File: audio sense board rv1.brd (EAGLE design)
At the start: 80 x 26.7 mm, 32 parts, among them IC2 TSOP38238, J1 PJRAN1X1U01X, J2 Debug Jumper, J4 PJRAN1X1U01X, Q1 2N3904, Q2 2N3904

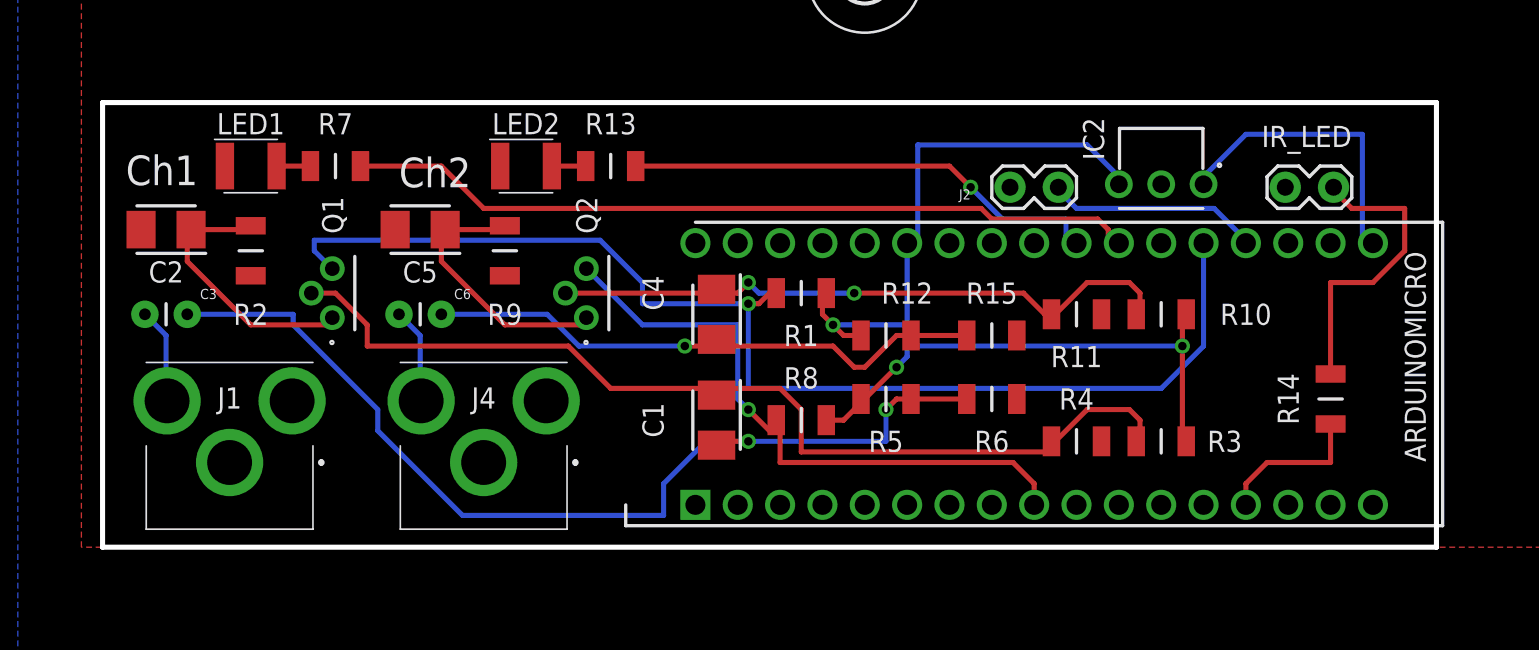
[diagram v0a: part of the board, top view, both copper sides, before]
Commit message: update resistors, corners
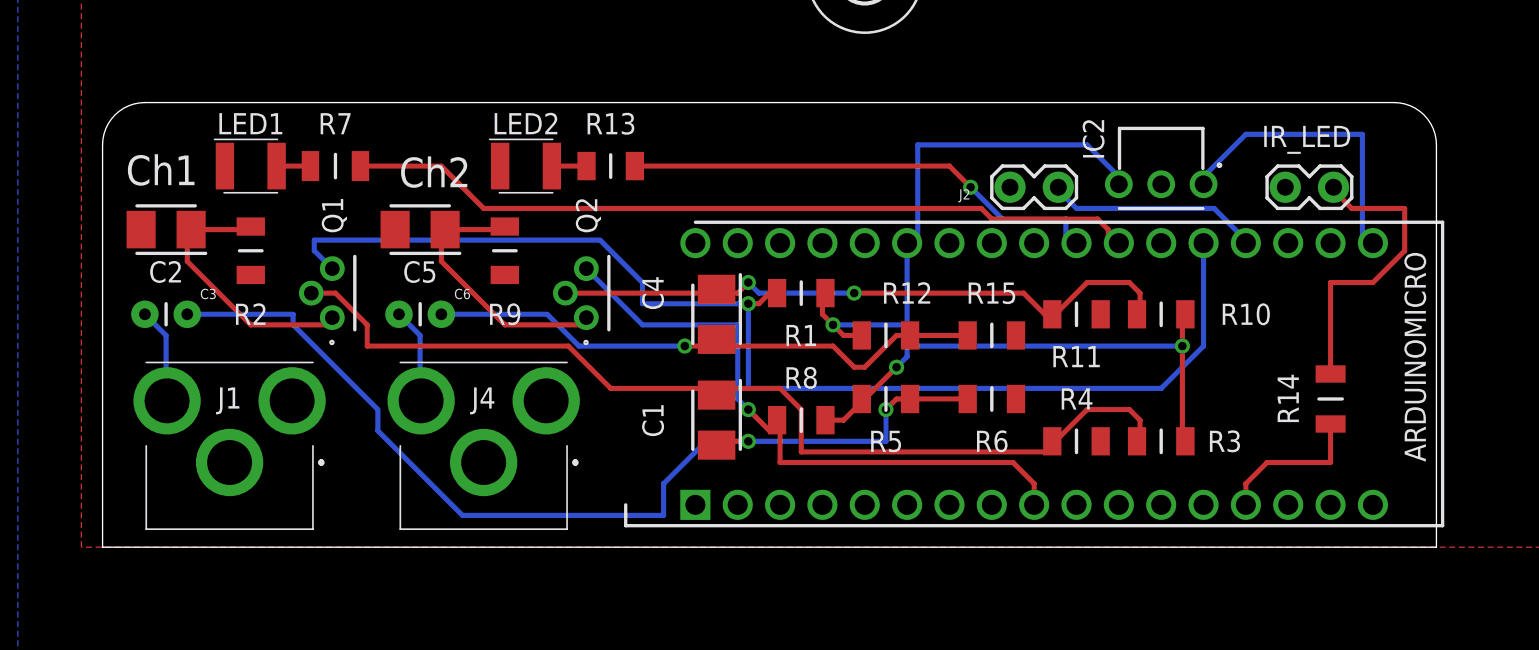
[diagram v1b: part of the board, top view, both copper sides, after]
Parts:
- R1, R10, R3, R8: device Samac Populated:RESC3216X60N@1 -> Samac Populated:RESC3116X70N
- R11, R12, R15, R2, R4, R5, R6, R9: device Samac Populated:RESC3216X60N -> Samac Populated:RESC3116X70N
- R13: value CRCW1206100RJNEAC -> ERJ8GEYJ101V; device Samac Populated:RESC3216X60N -> Samac Populated:RESC3116X70N
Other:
- outline, holes or cut-outs redrawn

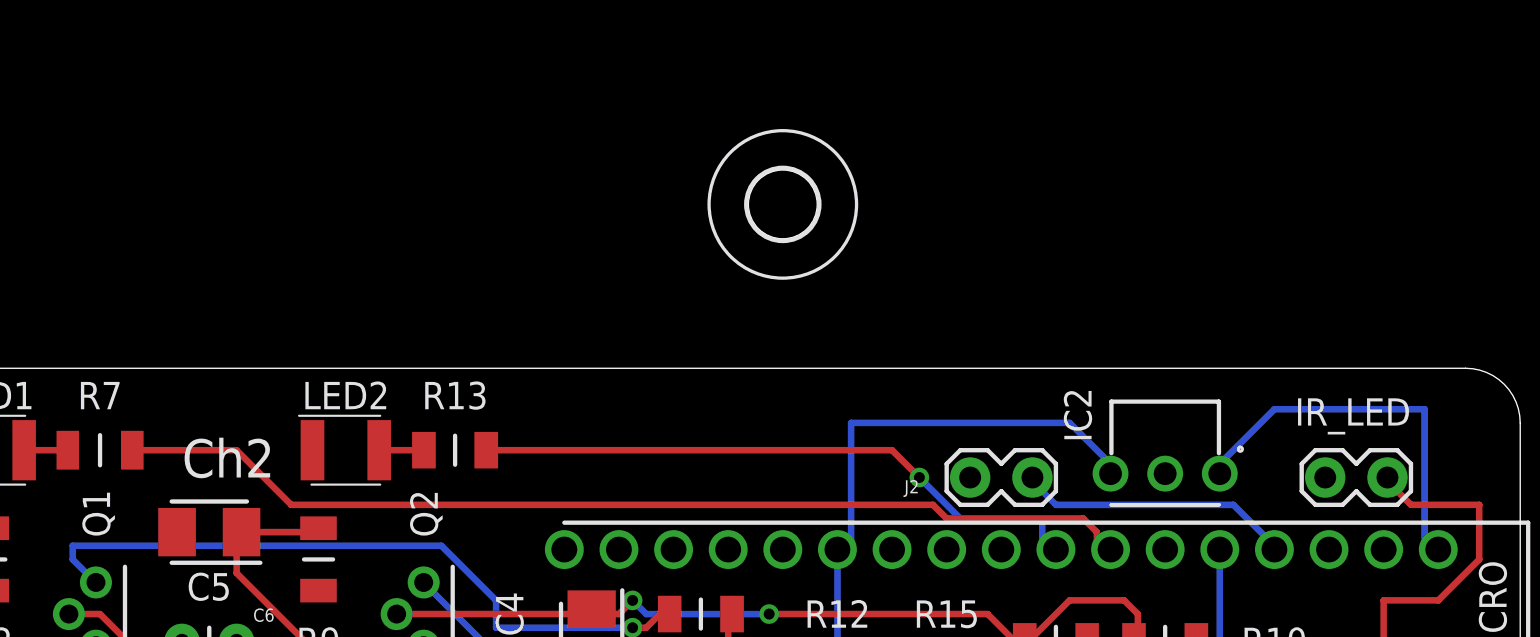
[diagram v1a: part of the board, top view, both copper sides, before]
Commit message: match LED names to channel names
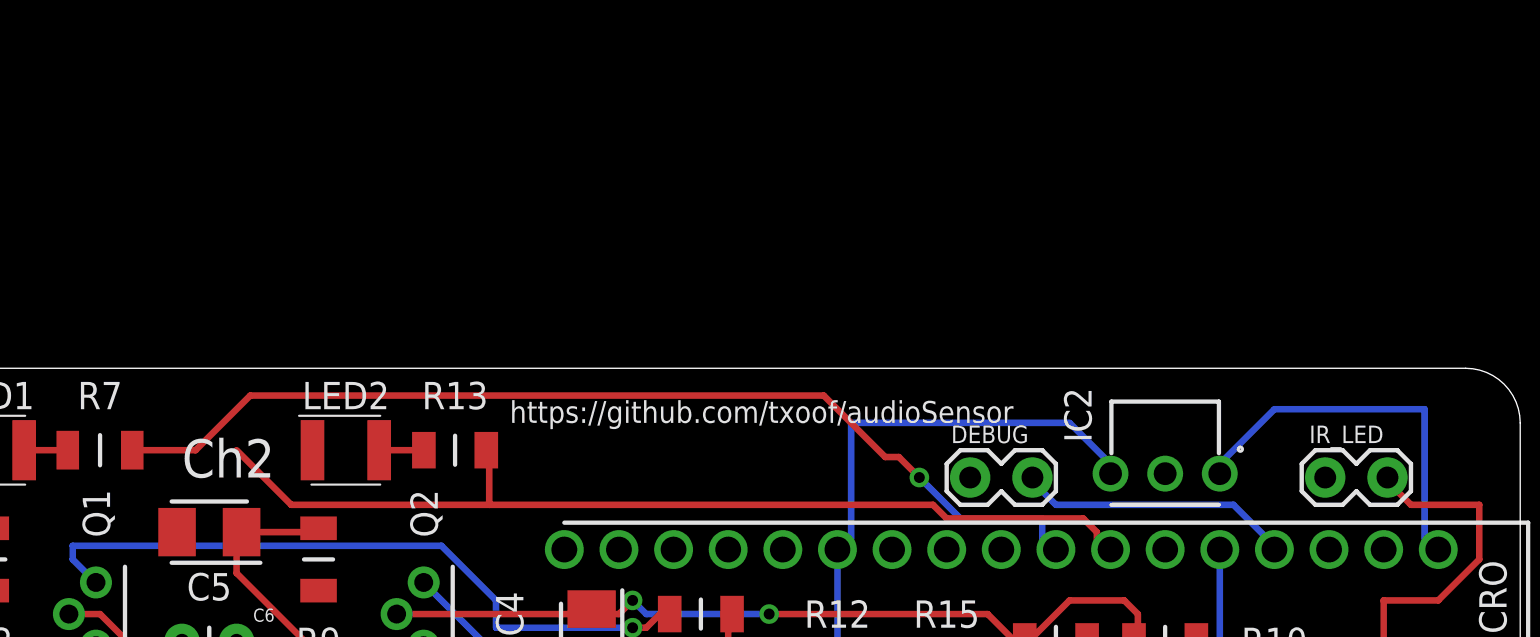
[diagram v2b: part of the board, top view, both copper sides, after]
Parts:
- removed U$3: (no value), holes:3,2
- renumbered J2 to DEBUG
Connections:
- net STATUS_CH1: now also R7.2; no longer R13.2
- net STATUS_CH2: now also R13.2; no longer R7.2
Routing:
- net STATUS_CH1: track 29.8 -> 48.4 mm
- net STATUS_CH2: track 47.9 -> 45.7 mm
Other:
- board text added: "https://github.com/txoof/audioSensor"
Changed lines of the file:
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@@
 <grid distance="50" unitdist="mil" unit="mil" style="lines" multiple="1" display="yes" altdistance="5" altunitdist="mil" altunit="mil"/>
 <layers>
-<layer number="1" name="Top" color="4" fill="1" visible="no" active="yes"/>
-<layer number="16" name="Bottom" color="1" fill="1" visible="no" active="yes"/>
-<layer number="17" name="Pads" color="2" fill="1" visible="no" active="yes"/>
-<layer number="18" name="Vias" color="2" fill="1" visible="no" active="yes"/>
-<layer number="19" name="Unrouted" color="6" fill="1" visible="no" active="yes"/>
+<layer number="1" name="Top" color="4" fill="1" visible="yes" active="yes"/>
+<layer number="16" name="Bottom" color="1" fill="1" visible="yes" active="yes"/>
+<layer number="17" name="Pads" color="2" fill="1" visible="yes" active="yes"/>
+<layer number="18" name="Vias" color="2" fill="1" visible="yes" active="yes"/>
+<layer number="19" name="Unrouted" color="6" fill="1" visible="yes" active="yes"/>
 <layer number="20" name="Dimension" color="24" fill="1" visible="yes" active="yes"/>
-<layer number="21" name="tPlace" color="7" fill="1" visible="no" active="yes"/>
-<layer number="22" name="bPlace" color="7" fill="1" visible="no" active="yes"/>
-<layer number="23" name="tOrigins" color="15" fill="1" visible="no" active="yes"/>
-<layer number="24" name="bOrigins" color="15" fill="1" visible="no" active="yes"/>
-<layer number="25" name="tNames" color="7" fill="1" visible="no" active="yes"/>
-<layer number="26" name="bNames" color="7" fill="1" visible="no" active="yes"/>
+<layer number="21" name="tPlace" color="7" fill="1" visible="yes" active="yes"/>
+<layer number="22" name="bPlace" color="7" fill="1" visible="yes" active="yes"/>
+<layer number="23" name="tOrigins" color="15" fill="1" visible="yes" active="yes"/>
+<layer number="24" name="bOrigins" color="15" fill="1" visible="yes" active="yes"/>
+<layer number="25" name="tNames" color="7" fill="1" visible="yes" active="yes"/>
+<layer number="26" name="bNames" color="7" fill="1" visible="yes" active="yes"/>
 <layer number="27" name="tValues" color="7" fill="1" visible="no" active="yes"/>
 <layer number="28" name="bValues" color="7" fill="1" visible="no" active="yes"/>
@@
 <layer number="37" name="tTest" color="7" fill="1" visible="no" active="yes"/>
 <layer number="38" name="bTest" color="7" fill="1" visible="no" active="yes"/>
-<layer number="39" name="tKeepout" color="4" fill="11" visible="no" active="yes"/>
-<layer number="40" name="bKeepout" color="1" fill="11" visible="no" active="yes"/>
-<layer number="41" name="tRestrict" color="4" fill="10" visible="no" active="yes"/>
-<layer number="42" name="bRestrict" color="1" fill="10" visible="no" active="yes"/>
+<layer number="39" name="tKeepout" color="4" fill="11" visible="yes" active="yes"/>
+<layer number="40" name="bKeepout" color="1" fill="11" visible="yes" active="yes"/>
+<layer number="41" name="tRestrict" color="4" fill="10" visible="yes" active="yes"/>
+<layer number="42" name="bRestrict" color="1" fill="10" visible="yes" active="yes"/>
 <layer number="43" name="vRestrict" color="2" fill="10" visible="no" active="yes"/>
 <layer number="44" name="Drills" color="7" fill="1" visible="no" active="yes"/>
@@
 <layer number="49" name="Reference" color="7" fill="1" visible="no" active="yes"/>
 <layer number="50" name="dxf" color="7" fill="1" visible="no" active="no"/>
-<layer number="51" name="tDocu" color="7" fill="1" visible="no" active="yes"/>
-<layer number="52" name="bDocu" color="7" fill="1" visible="no" active="yes"/>
+<layer number="51" name="tDocu" color="7" fill="1" visible="yes" active="yes"/>
+<layer number="52" name="bDocu" color="7" fill="1" visible="yes" active="yes"/>
 <layer number="53" name="tGND_GNDA" color="7" fill="9" visible="no" active="no"/>
 <layer number="54" name="bGND_GNDA" color="1" fill="9" visible="no" active="no"/>
@@
 <wire x1="80.01" y1="24.13" x2="80.01" y2="0" width="0.002540625" layer="20"/>
 <wire x1="80.01" y1="0" x2="0" y2="0" width="0.002540625" layer="20"/>
-<dimension x1="0" y1="0" x2="80.01" y2="0" x3="87.81" y3="0" textsize="1.778" layer="20" dtype="radius"/>
-<dimension x1="0" y1="26.67" x2="0" y2="0.000003125" x3="0" y3="-7.799996875" textsize="1.778" layer="20" dtype="radius"/>
+<text x="33.02" y="24.13" size="1.016" layer="25">https://github.com/txoof/audioSensor</text>
 </plain>
 <attributes>
@@
 </element>
 <element name="IR_LED" library="SparkFun-Connectors" library_urn="urn:adsk.eagle:library:513" package="1X02_LOCK" package3d_urn="urn:adsk.eagle:package:38045/1" value="IR LED connection" x="73.66" y="21.59" smashed="yes" rot="R180">
-<attribute name="NAME" x="74.93" y="25.273" size="1.27" layer="25" font="vector" ratio="20" rot="R180"/>
+<attribute name="NAME" x="73.66" y="24.003" size="0.8128" layer="25" font="vector" ratio="20" rot="R180"/>
 <attribute name="VALUE" x="74.93" y="23.622" size="0.6096" layer="27" font="vector" ratio="20" rot="R180"/>
 </element>
@@
 <attribute name="VALUE" x="24.13" y="17.78" size="1.27" layer="27" rot="R270" align="center"/>
 </element>
-<element name="U$3" library="holes" library_urn="urn:adsk.eagle:library:237" package="3,2" package3d_urn="urn:adsk.eagle:package:14275/1" value="" x="45.72" y="34.29" smashed="yes"/>
-<element name="J2" library="SparkFun-Connectors" library_urn="urn:adsk.eagle:library:513" package="1X02_LOCK" package3d_urn="urn:adsk.eagle:package:38045/1" value="Debug Jumper" x="54.61" y="21.59" smashed="yes">
-<attribute name="NAME" x="52.07" y="21.463" size="0.6096" layer="25" font="vector" ratio="20" rot="R180"/>
+<element name="DEBUG" library="SparkFun-Connectors" library_urn="urn:adsk.eagle:library:513" package="1X02_LOCK" package3d_urn="urn:adsk.eagle:package:38045/1" value="Debug Jumper" x="54.61" y="21.59" smashed="yes">
+<attribute name="NAME" x="57.15" y="24.003" size="0.8128" layer="25" font="vector" ratio="20" rot="R180"/>
 <attribute name="VALUE" x="53.34" y="19.558" size="0.6096" layer="27" font="vector" ratio="20"/>
 </element>
@@
 <vertex x="121.92" y="69.85"/>
 </polygon>
-<contactref element="J2" pad="1"/>
+<contactref element="DEBUG" pad="1"/>
 <contactref element="LED1" pad="1"/>
 <contactref element="LED2" pad="1"/>
@@
 </signal>
 <signal name="DEBUGJ">
-<contactref element="J2" pad="2"/>
+<contactref element="DEBUG" pad="2"/>
 <contactref element="ARDUINOMICRO" pad="21"/>
 <wire x1="66.675" y1="20.32" x2="68.58" y2="18.415" width="0.3048" layer="16"/>
@@
 </signal>
 <signal name="STATUS_CH1">
-<contactref element="R13" pad="2"/>
 <contactref element="ARDUINOMICRO" pad="25"/>
-<wire x1="50.8" y1="22.86" x2="31.93" y2="22.86" width="0.3048" layer="1"/>
-<wire x1="52.07" y1="21.59" x2="50.8" y2="22.86" width="0.3048" layer="1"/>
+<wire x1="52.07" y1="21.59" x2="51.1175" y2="22.5425" width="0.3048" layer="1"/>
 <wire x1="53.975" y1="19.685" x2="52.07" y2="21.59" width="0.3048" layer="16"/>
 <wire x1="57.785" y1="19.685" x2="53.975" y2="19.685" width="0.3048" layer="16"/>
@@
 <wire x1="58.42" y1="17.78" x2="58.42" y2="18.24" width="0.3048" layer="16"/>
 <via x="52.07" y="21.59" extent="1-16" drill="0.508"/>
+<contactref element="R7" pad="2"/>
+<wire x1="18.415" y1="22.86" x2="15.47" y2="22.86" width="0.3048" layer="1"/>
+<wire x1="20.955" y1="25.4" x2="18.415" y2="22.86" width="0.3048" layer="1"/>
+<wire x1="47.625" y1="25.4" x2="20.955" y2="25.4" width="0.3048" layer="1"/>
+<wire x1="50.4825" y1="22.5425" x2="47.625" y2="25.4" width="0.3048" layer="1"/>
+<wire x1="51.1175" y1="22.5425" x2="50.4825" y2="22.5425" width="0.3048" layer="1"/>
 </signal>
 <signal name="STATUS_CH2">
-<contactref element="R7" pad="2"/>
 <contactref element="ARDUINOMICRO" pad="24"/>
-<wire x1="20.32" y1="22.86" x2="15.47" y2="22.86" width="0.3048" layer="1"/>
 <wire x1="22.86" y1="20.32" x2="20.32" y2="22.86" width="0.3048" layer="1"/>
-<wire x1="52.705" y1="20.32" x2="22.86" y2="20.32" width="0.3048" layer="1"/>
+<wire x1="52.705" y1="20.32" x2="32.0675" y2="20.32" width="0.3048" layer="1"/>
+<wire x1="32.0675" y1="20.32" x2="22.86" y2="20.32" width="0.3048" layer="1"/>
 <wire x1="53.34" y1="19.685" x2="52.705" y2="20.32" width="0.3048" layer="1"/>
 <wire x1="59.69" y1="19.685" x2="53.34" y2="19.685" width="0.3048" layer="1"/>
@@
 <wire x1="60.96" y1="18.415" x2="60.325" y2="18.415" width="0.3048" layer="1"/>
 <wire x1="60.96" y1="18.415" x2="60.96" y2="18.24" width="0.3048" layer="1"/>
+<contactref element="R13" pad="2"/>
+<wire x1="32.0675" y1="20.32" x2="32.0675" y2="22.86" width="0.3048" layer="1"/>
+<wire x1="32.0675" y1="22.86" x2="31.93" y2="22.86" width="0.3048" layer="1"/>
 </signal>
 <signal name="IRLED">
